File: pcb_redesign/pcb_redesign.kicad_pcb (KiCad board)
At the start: 2 copper layers, 22 parts, among them J1 USB_B_Mini, U1 ESP32-S3-WROOM-1, U3 SPX1117M3-L-3-3/TR

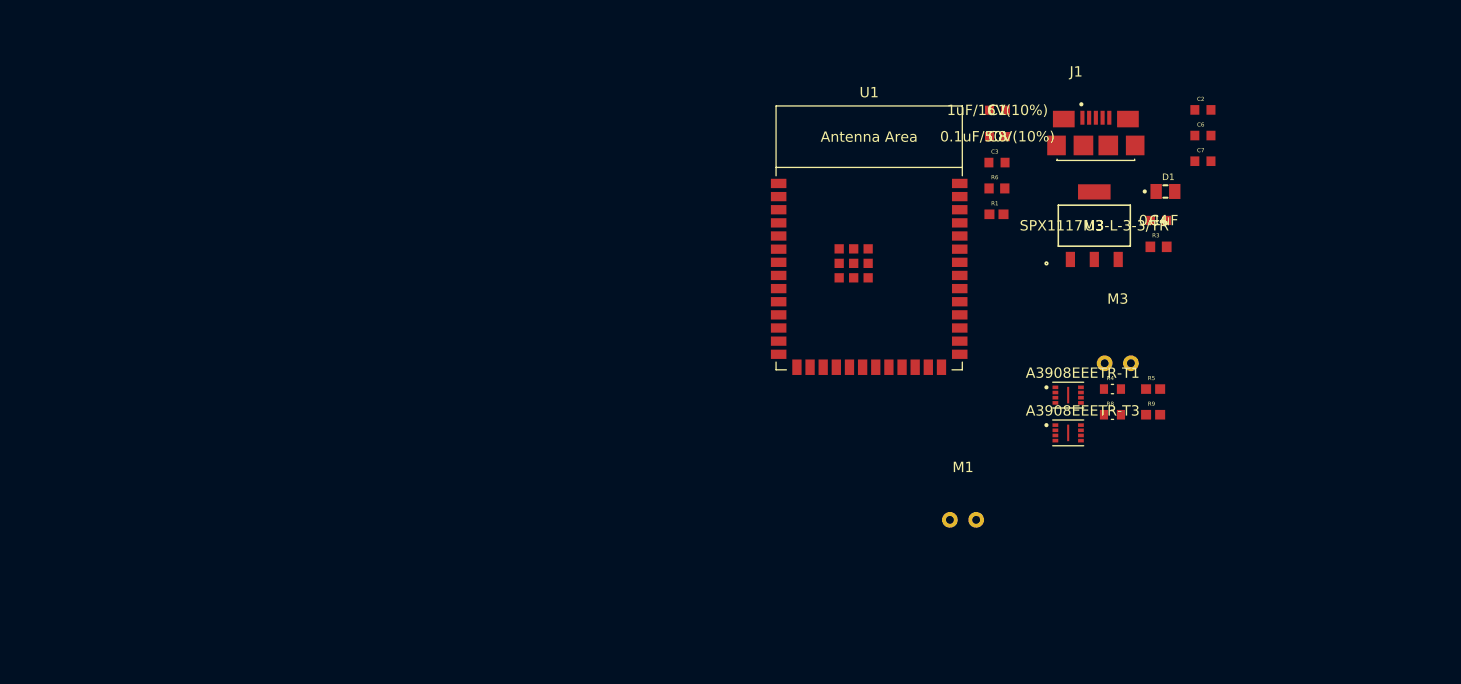
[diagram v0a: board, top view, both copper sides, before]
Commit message: added outline in pcb editor
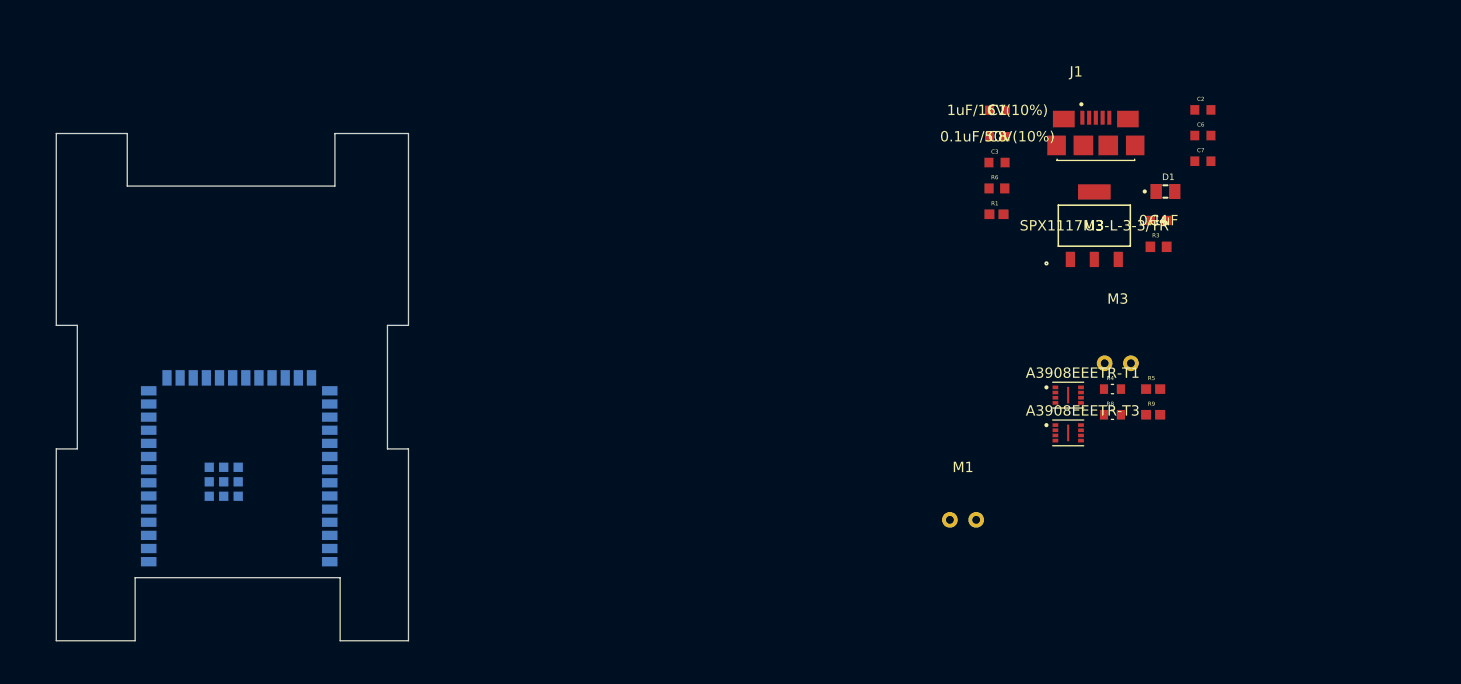
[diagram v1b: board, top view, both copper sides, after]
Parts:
- U1: moved to B.Cu
- moved U1 64.1 mm to (38.0, 99.9)
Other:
- board outline added: 34 x 49 mm

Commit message: components added to board
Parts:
- removed J1: USB_B_Mini, micro_usb_type_b:AMPHENOL_10118192-0002LF
- added J2: USB_B, micro_usb_type_b:AMPHENOL_10118192-0002LF, F.Cu at (50.3, 79.2)
- added JP1: SolderJumper_2_Open, Jumper:SolderJumper-2_P1.3mm_Open_Pad1.0x1.5mm, F.Cu at (25.9, 96.0)
- D1: footprint green_LED:LEDC2012X70N -> LED_SMD:LED_0805_2012Metric
- moved M3 101.2 mm to (23.6, 63.9)
- moved R9 100.5 mm to (26.7, 81.3), turned to -90 degrees
- moved C6 98.6 mm to (33.8, 82.8)
- moved C7 98.5 mm to (33.8, 84.6)
- moved A3908EEETR-T3 97.2 mm to (23.1, 74.9)
- moved R8 97.2 mm to (26.7, 77.2), turned to -90 degrees
- moved C1 97.1 mm to (25.9, 110.7)
- moved R6 93.2 mm to (22.9, 101.9), turned to -90 degrees
- moved R1 91.9 mm to (25.9, 109.0)
- moved C8 90.0 mm to (24.1, 89.7)
- moved R3 90.0 mm to (37.1, 84.6)
- moved C3 89.0 mm to (24.1, 87.9)
- moved C2 86.5 mm to (47.5, 86.6)
- moved D1 86.5 mm to (41.9, 84.8)
- moved U3 85.2 mm to (35.5, 77.2), turned to 180 degrees
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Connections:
- A3908EEETR-T1 pad 3: unconnected-(A3908EEETR-T1-VDD-Pad3) -> 3.7_UNREG
- A3908EEETR-T1 pad 5: ENB Right motor -> ENA Right Motor
- A3908EEETR-T1 pad 6: ENA Right motor -> ENB Right Motor
- A3908EEETR-T3 pad 3: unconnected-(A3908EEETR-T3-VDD-Pad3) -> 3.7_UNREG
- A3908EEETR-T3 pad 5: ENA Left motor -> ENA Left Motor
- A3908EEETR-T3 pad 6: ENA Left motor -> ENB Left Motor
- C1 pad 1: Net-(C1-Pad1) -> /CHIP_PU
- C2 pad 2: Net-(J1-VBUS) -> 3.7_UNREG
- C3 pad 2: Net-(C3-Pad2) -> VCC_3V3
- C4 pad 2: Net-(J1-VBUS) -> 3.7_UNREG
- C6 pad 2: Net-(U3-EPAD) -> VCC_3V3
- C7 pad 2: Net-(U3-EPAD) -> VCC_3V3
- C8 pad 2: Net-(C3-Pad2) -> VCC_3V3
- R1 pad 1: unconnected-(R1-Pad1) -> /ESP32_3V3
- R1 pad 2: Net-(C1-Pad1) -> /CHIP_PU
- R3 pad 1: Net-(J1-VBUS) -> 3.7_UNREG
- R6 pad 1: Net-(C3-Pad2) -> VCC_3V3
- R6 pad 2: Net-(U1-3V3) -> /ESP32_3V3
- U1 pad 10: unconnected-(U1-GPIO17/U1TXD/ADC2_CH6-Pad10) -> Net-(JP1-B)
- U1 pad 11: unconnected-(U1-GPIO18/U1RXD/ADC2_CH7/CLK_OUT3-Pad11) -> Net-(JP1-A)
- U1 pad 2: Net-(U1-3V3) -> /ESP32_3V3
- U1 pad 3: unconnected-(U1-EN-Pad3) -> /CHIP_PU
- U3 pad 2: Net-(U3-EPAD) -> VCC_3V3
- U3 pad 3: Net-(J1-VBUS) -> 3.7_UNREG
- U3 pad 4: Net-(U3-EPAD) -> VCC_3V3

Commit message: switching to laptop
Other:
- copper layers 2 -> 4
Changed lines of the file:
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@@
   (layers
     (0 "F.Cu" signal)
+    (1 "In1.Cu" signal)
+    (2 "In2.Cu" signal)
     (31 "B.Cu" power)
     (32 "B.Adhes" user "B.Adhesive")
@@
       (layer "F.Mask" (type "Top Solder Mask") (thickness 0.01))
       (layer "F.Cu" (type "copper") (thickness 0.035))
-      (layer "dielectric 1" (type "core") (thickness 1.51) (material "FR4") (epsilon_r 4.5) (loss_tangent 0.02))
+      (layer "dielectric 1" (type "prepreg") (thickness 0.1) (material "FR4") (epsilon_r 4.5) (loss_tangent 0.02))
+      (layer "In1.Cu" (type "copper") (thickness 0.035))
+      (layer "dielectric 2" (type "core") (thickness 1.24) (material "FR4") (epsilon_r 4.5) (loss_tangent 0.02))
+      (layer "In2.Cu" (type "copper") (thickness 0.035))
+      (layer "dielectric 3" (type "prepreg") (thickness 0.1) (material "FR4") (epsilon_r 4.5) (loss_tangent 0.02))
       (layer "B.Cu" (type "copper") (thickness 0.035))
       (layer "B.Mask" (type "Bottom Solder Mask") (thickness 0.01))

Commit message: added layers and filled the board
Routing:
- added copper zone on In1.Cu, net GND
- added copper zone on In2.Cu, net VCC_3V3
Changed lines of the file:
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@@
   (layers
     (0 "F.Cu" signal)
-    (1 "In1.Cu" signal)
-    (2 "In2.Cu" signal)
-    (31 "B.Cu" power)
+    (1 "In1.Cu" power "GND")
+    (2 "In2.Cu" power "3.3V _REG")
+    (31 "B.Cu" signal)
     (32 "B.Adhes" user "B.Adhesive")
     (33 "F.Adhes" user "F.Adhesive")
@@
   (gr_line (start 47.244 66.802) (end 47.244 71.882)
     (stroke (width 0.1) (type default)) (layer "Edge.Cuts"))
+  (zone (net 2) (net_name "GND") (layer "In1.Cu") (hatch edge 0.5)
+    (connect_pads (clearance 0.508))
+    (min_thickness 0.25) (filled_areas_thickness no)
+    (fill (thermal_gap 0.5) (thermal_bridge_width 0.5))
+    (polygon
+      (pts
+        (xy 20.828 67.31)
+        (xy 26.67 67.31)
+        (xy 26.67 72.644)
+        (xy 47.498 72.39)
+        (xy 47.498 67.056)
+        (xy 54.102 67.056)
+        (xy 54.102 84.836)
+        (xy 51.562 84.836)
+        (xy 51.562 97.79)
+        (xy 53.848 97.79)
+        (xy 53.848 115.316)
+        (xy 48.514 115.316)
+        (xy 48.514 109.22)
+        (xy 27.432 109.22)
+        (xy 27.432 115.062)
+        (xy 20.828 115.062)
+        (xy 20.828 98.044)
+        (xy 22.86 98.044)
+        (xy 22.86 84.836)
+        (xy 20.828 84.836)
+      )
+    )
+  )
+  (zone (net 49) (net_name "VCC_3V3") (layer "In2.Cu") (hatch edge 0.5)
+    (priority 1)
+    (connect_pads (clearance 0.508))
+    (min_thickness 0.25) (filled_areas_thickness no)
+    (fill (thermal_gap 0.5) (thermal_bridge_width 0.5))
+    (polygon
+      (pts
+        (xy 20.828 67.31)
+        (xy 26.67 67.31)
+        (xy 26.67 72.644)
+        (xy 47.498 72.39)
+        (xy 47.498 67.056)
+        (xy 54.102 67.056)
+        (xy 54.102 84.836)
+        (xy 51.562 84.836)
+        (xy 51.562 97.79)
+        (xy 53.848 97.79)
+        (xy 53.848 115.316)
+        (xy 48.514 115.316)
+        (xy 48.514 109.22)
+        (xy 27.432 109.22)
+        (xy 27.432 115.062)
+        (xy 20.828 115.062)
+        (xy 20.828 98.044)
+        (xy 22.86 98.044)
+        (xy 22.86 84.836)
+        (xy 20.828 84.836)
+      )
+    )
+  )
 )

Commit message: switching to laptop
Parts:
- U1: moved to F.Cu
- moved J2 25.9 mm to (24.4, 80.0), turned to -90 degrees
- moved A3908EEETR-T3 18.1 mm to (40.9, 78.2)
- moved R9 17.3 mm to (42.9, 75.4), turned to 0 degrees
- moved R8 16.6 mm to (42.9, 73.7), turned to 0 degrees
- moved U3 6.78 mm to (30.7, 82.0)
- moved R5 6.65 mm to (53.1, 80.5)
- moved R4 6.60 mm to (53.1, 77.5)
- moved A3908EEETR-T1 5.39 mm to (48.5, 74.9)
- moved C6 2.75 mm to (35.3, 85.1)
- moved C7 2.75 mm to (35.3, 86.9)
- moved R3 2.75 mm to (38.6, 86.9)
- moved D1 1.91 mm to (42.6, 86.6)
- moved JP1 0.76 mm to (26.7, 96.0)
- moved C3 0.25 mm to (24.4, 87.9)
- moved C8 0.25 mm to (24.4, 89.7)
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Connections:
- A3908EEETR-T3 pad 3: 3.7_UNREG -> VCC_3V3
- U1 pad 38: ENB Right Motor -> ENB Left Motor
- U1 pad 39: ENA Right Motor -> ENA Left Motor
- U1 pad 4: ENA Left Motor -> ENB Right Motor
- U1 pad 5: ENB Left Motor -> ENA Right Motor
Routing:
- net ENB Right Motor: track 0.00 -> 31.8 mm
- net ENA Right Motor: track 0.00 -> 29.2 mm
- net 3.7_UNREG: track 0.00 -> 4.07 mm
- net Net-(A3908EEETR-T3-OUTA): track 0.00 -> 0.81 mm

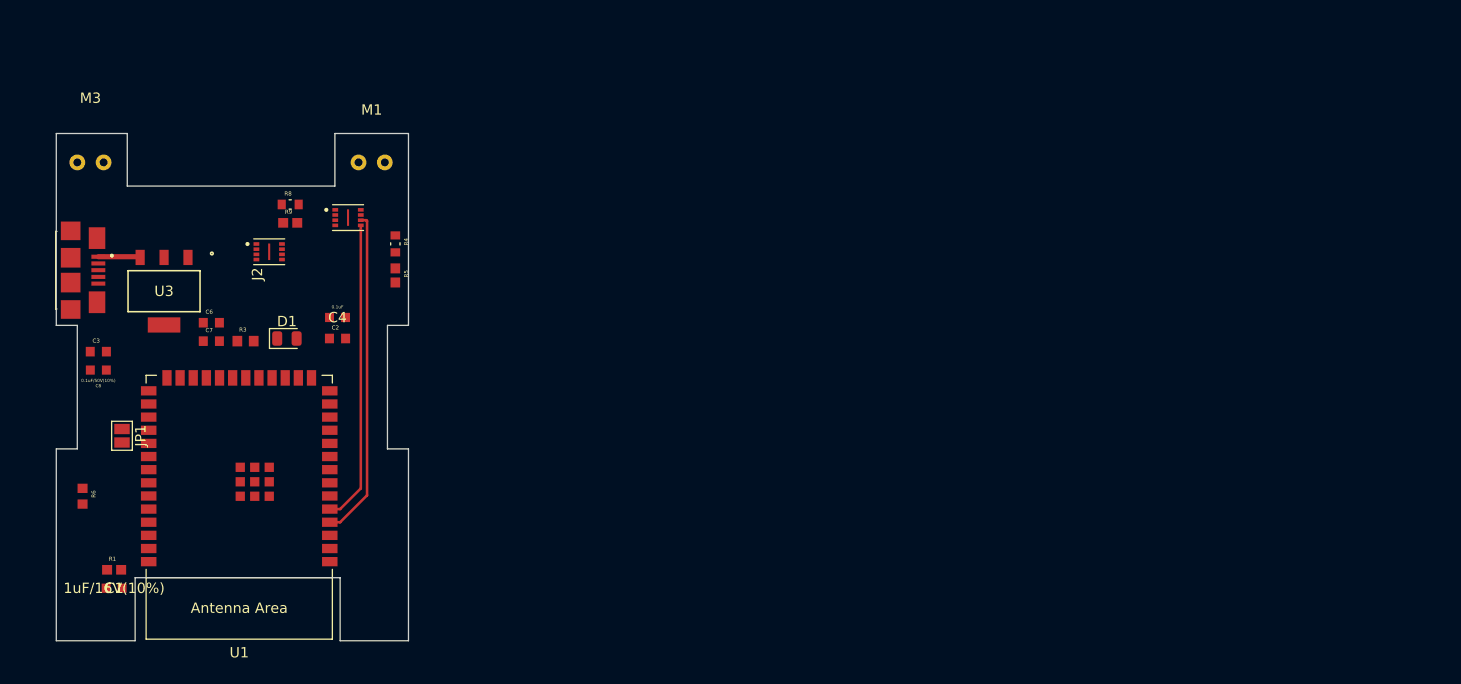
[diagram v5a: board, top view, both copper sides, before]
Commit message: wired up 2.13
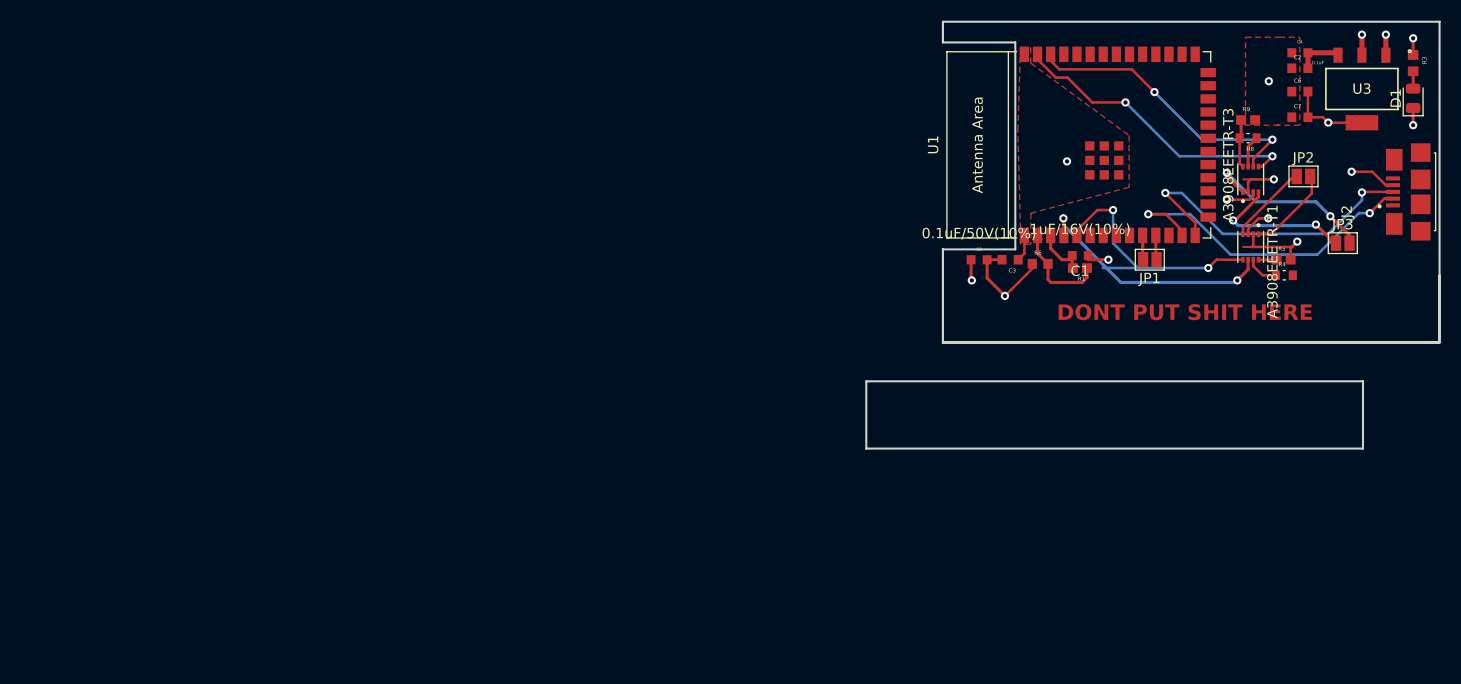
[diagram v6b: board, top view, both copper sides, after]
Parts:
- removed M1, M3: ~, motor:motor
- added JP2: SolderJumper_2_Open, Jumper:SolderJumper-2_P1.3mm_Open_Pad1.0x1.5mm, F.Cu at (140.8, 71.0)
- added JP3: SolderJumper_2_Open, Jumper:SolderJumper-2_P1.3mm_Open_Pad1.0x1.5mm, F.Cu at (144.7, 77.4)
- R4, R8: value 18k -> 30k
- moved J2 125.3 mm to (149.5, 72.4), turned to 90 degrees
- moved U3 117.4 mm to (146.5, 62.5)
- moved R3 116.0 mm to (151.4, 60.0), turned to -90 degrees
- moved D1 111.3 mm to (151.4, 63.4), turned to 90 degrees
- moved C6 107.5 mm to (140.5, 62.8)
- moved C7 107.4 mm to (140.5, 65.2)
- moved JP1 100.8 mm to (126.0, 79.0), turned to 180 degrees
- moved C1 98.7 mm to (119.3, 78.6)
- moved R1 97.8 mm to (119.2, 79.8), turned to 180 degrees
- moved C2 96.6 mm to (140.5, 60.5)
- moved C4 96.5 mm to (140.5, 59.0)
- moved R6 95.2 mm to (115.4, 79.4), turned to 0 degrees
- moved A3908EEETR-T3 95.1 mm to (135.8, 71.2), turned to 90 degrees
- moved R9 93.1 mm to (135.5, 65.5)
- moved R8 92.8 mm to (135.5, 67.2), turned to 180 degrees
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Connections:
- R3 pad 1: 3.7_UNREG -> VCC_3V3
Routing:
- net D-: track 0.00 -> 31.9 mm, vias 0 -> 2
- net D+: track 0.00 -> 31.1 mm, vias 0 -> 2
- net ENA Left Motor: track 0.00 -> 28.8 mm, vias 0 -> 2
- net ENB Left Motor: track 0.00 -> 28.6 mm, vias 0 -> 2
- net GND: track 0.00 -> 26.3 mm, vias 0 -> 9
- net VCC_3V3: track 0.00 -> 24.4 mm, vias 0 -> 5
- net Net-(A3908EEETR-T3-OUTB): track 0.48 -> 17.6 mm, vias 0 -> 2
- net Net-(A3908EEETR-T3-OUTA): track 0.81 -> 14.8 mm, vias 0 -> 2
- net /ESP32_3V3: track 0.00 -> 10.2 mm
- net Net-(A3908EEETR-T1-OUTB): track 0.00 -> 8.49 mm
- net Net-(A3908EEETR-T1-OUTA): track 0.00 -> 7.91 mm
- net ENB Right Motor: track 31.8 -> 23.9 mm, vias 0 -> 2
- net /CHIP_PU: track 0.00 -> 5.08 mm
- net Net-(A3908EEETR-T3-VSET): track 0.00 -> 4.94 mm
- net ENA Right Motor: track 29.2 -> 25.3 mm, vias 0 -> 2
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- added copper zone on F.Cu, net GND
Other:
- board size 34 x 49 mm -> 55.4 x 41.2 mm
- board text added: "DONT PUT SHIT HERE"

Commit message: getting lunch
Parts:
- moved C2 2.29 mm to (138.2, 60.8)
- moved C4 2.29 mm to (138.2, 59.3)
- moved C6 2.29 mm to (138.2, 63.0)
- moved C7 2.29 mm to (138.2, 65.5)
- moved U3 2.29 mm to (144.2, 62.8), turned to 0 degrees
- moved R4 1.03 mm to (138.2, 81.2), turned to 90 degrees
- moved R1 0.40 mm to (119.2, 80.2)
- moved R6 0.25 mm to (115.7, 79.4)
- moved R9 0.25 mm to (135.2, 65.5)
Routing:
- net 3.7_UNREG: track 7.39 -> 38.4 mm
- net VCC_3V3: track 24.4 -> 31.2 mm, vias 5 -> 4
- net GND: track 26.3 -> 32.2 mm, vias 9 -> 8
- net ENA Right Motor: track 25.3 -> 21.9 mm
- net D-: track 31.9 -> 34.1 mm
- net Net-(A3908EEETR-T1-VSET): track 1.83 -> 3.21 mm
- net ENB Right Motor: track 23.9 -> 25.2 mm
- net Net-(A3908EEETR-T1-VREF): track 3.16 -> 3.95 mm

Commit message: finished design
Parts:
- removed U3: SPX1117M3-L-3-3/TR, 3.3v_reg:SPX1117M3-L-3-3&slash_TR
- added IC1: SPX1117M3-L-3-3_TR, 3.3v_reg:SOT230P700X180-4N, F.Cu at (144.2, 62.4)
- C1, C4, C8: footprint 1uF_cap_0603:CL10A105KB8NNNC -> Capacitor_SMD:C_0603_1608Metric
- Motor L: renamed from JP3
- Motor R: renamed from JP2
- moved J2 0.12 mm to (149.4, 72.4)
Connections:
- A3908EEETR-T1 pad 3: 3.7_UNREG -> VCC_3V3
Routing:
- net 3.7_UNREG: track 38.4 -> 34.1 mm, vias 1 -> 0
- net VCC_3V3: track 31.2 -> 34.0 mm, vias 4 -> 6
- net /ESP32_3V3: track 10.2 -> 9.34 mm
- net GND: track 32.2 -> 31.6 mm
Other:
- board size 55.4 x 41.2 mm -> 48 x 31 mm
